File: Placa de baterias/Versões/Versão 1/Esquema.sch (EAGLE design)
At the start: 3 parts

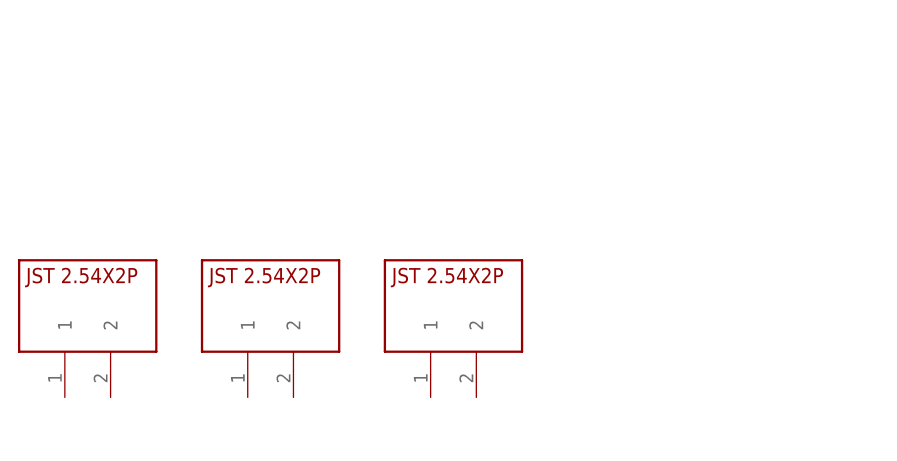
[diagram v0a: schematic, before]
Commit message: mudanças na placa de processamento
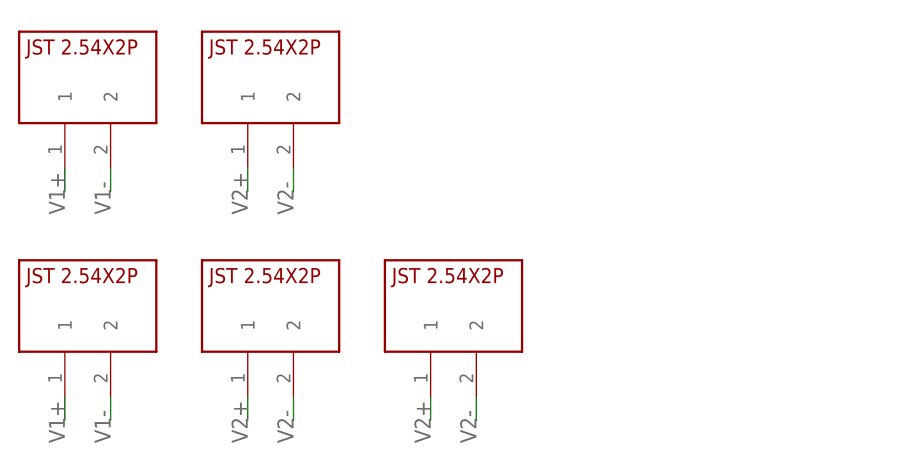
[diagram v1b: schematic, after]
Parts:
- added U$4, U$5: JST2.54X2P, CRD:JST2.54X2P
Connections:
- new net V1+: U$1.1, U$4.1
- new net V1-: U$1.2, U$4.2
- new net V2+: U$2.1, U$3.1, U$5.1
- new net V2-: U$2.2, U$3.2, U$5.2
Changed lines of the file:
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@@
 <part name="U$2" library="CRD" library_urn="urn:adsk.eagle:library:39051337" deviceset="JST2.54X2P" device="" package3d_urn="urn:adsk.eagle:package:39191967/2"/>
 <part name="U$3" library="CRD" library_urn="urn:adsk.eagle:library:39051337" deviceset="JST2.54X2P" device="" package3d_urn="urn:adsk.eagle:package:39191967/2"/>
+<part name="U$4" library="CRD" library_urn="urn:adsk.eagle:library:39051337" deviceset="JST2.54X2P" device="" package3d_urn="urn:adsk.eagle:package:39191967/2"/>
+<part name="U$5" library="CRD" library_urn="urn:adsk.eagle:library:39051337" deviceset="JST2.54X2P" device="" package3d_urn="urn:adsk.eagle:package:39191967/2"/>
 </parts>
 <sheets>
@@
 <instance part="U$2" gate="G$1" x="0" y="0" smashed="yes"/>
 <instance part="U$3" gate="G$1" x="20.32" y="0" smashed="yes"/>
+<instance part="U$4" gate="G$1" x="-20.32" y="25.4" smashed="yes"/>
+<instance part="U$5" gate="G$1" x="0" y="25.4" smashed="yes"/>
 </instances>
 <busses>
 </busses>
 <nets>
+<net name="V1+" class="0">
+<segment>
+<pinref part="U$4" gate="G$1" pin="1"/>
+<wire x1="-22.86" y1="15.24" x2="-22.86" y2="12.7" width="0.1524" layer="91"/>
+<label x="-22.86" y="10.16" size="1.778" layer="95" rot="R90"/>
+</segment>
+<segment>
+<pinref part="U$1" gate="G$1" pin="1"/>
+<wire x1="-22.86" y1="-10.16" x2="-22.86" y2="-12.7" width="0.1524" layer="91"/>
+<label x="-22.86" y="-15.24" size="1.778" layer="95" rot="R90"/>
+</segment>
+</net>
+<net name="V1-" class="0">
+<segment>
+<pinref part="U$4" gate="G$1" pin="2"/>
+<wire x1="-17.78" y1="15.24" x2="-17.78" y2="12.7" width="0.1524" layer="91"/>
+<label x="-17.78" y="10.16" size="1.778" layer="95" rot="R90"/>
+</segment>
+<segment>
+<pinref part="U$1" gate="G$1" pin="2"/>
+<wire x1="-17.78" y1="-10.16" x2="-17.78" y2="-12.7" width="0.1524" layer="91"/>
+<label x="-17.78" y="-15.24" size="1.778" layer="95" rot="R90"/>
+</segment>
+</net>
+<net name="V2+" class="0">
+<segment>
+<pinref part="U$5" gate="G$1" pin="1"/>
+<wire x1="-2.54" y1="15.24" x2="-2.54" y2="12.7" width="0.1524" layer="91"/>
+<label x="-2.54" y="10.16" size="1.778" layer="95" rot="R90"/>
+</segment>
+<segment>
+<pinref part="U$2" gate="G$1" pin="1"/>
+<wire x1="-2.54" y1="-10.16" x2="-2.54" y2="-12.7" width="0.1524" layer="91"/>
+<label x="-2.54" y="-15.24" size="1.778" layer="95" rot="R90"/>
+</segment>
+<segment>
+<pinref part="U$3" gate="G$1" pin="1"/>
+<wire x1="17.78" y1="-10.16" x2="17.78" y2="-12.7" width="0.1524" layer="91"/>
+<label x="17.78" y="-15.24" size="1.778" layer="95" rot="R90"/>
+</segment>
+</net>
+<net name="V2-" class="0">
+<segment>
+<pinref part="U$5" gate="G$1" pin="2"/>
+<wire x1="2.54" y1="15.24" x2="2.54" y2="12.7" width="0.1524" layer="91"/>
+<label x="2.54" y="10.16" size="1.778" layer="95" rot="R90"/>
+</segment>
+<segment>
+<pinref part="U$2" gate="G$1" pin="2"/>
+<wire x1="2.54" y1="-10.16" x2="2.54" y2="-12.7" width="0.1524" layer="91"/>
+<label x="2.54" y="-15.24" size="1.778" layer="95" rot="R90"/>
+</segment>
+<segment>
+<pinref part="U$3" gate="G$1" pin="2"/>
+<wire x1="22.86" y1="-10.16" x2="22.86" y2="-12.7" width="0.1524" layer="91"/>
+<label x="22.86" y="-15.24" size="1.778" layer="95" rot="R90"/>
+</segment>
+</net>
 </nets>
 </sheet>

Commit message: atualização placa de baterias
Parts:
- added V: 22-23-2041, con-molex:22-23-2041
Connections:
- net V1+: now also V-3.S
- net V1-: now also V-4.S
- net V2+: now also V-2.S
- net V2-: now also V-1.S
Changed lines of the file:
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@@
 <drawing>
 <settings>
-<setting alwaysvectorfont="yes"/>
+<setting alwaysvectorfont="no"/>
 <setting verticaltext="up"/>
 </settings>
@@
 <part name="U$4" library="CRD" library_urn="urn:adsk.eagle:library:39051337" deviceset="JST2.54X2P" device="" package3d_urn="urn:adsk.eagle:package:39191967/2"/>
 <part name="U$5" library="CRD" library_urn="urn:adsk.eagle:library:39051337" deviceset="JST2.54X2P" device="" package3d_urn="urn:adsk.eagle:package:39191967/2"/>
+<part name="V" library="con-molex" library_urn="urn:adsk.eagle:library:165" deviceset="22-23-2041" device="" package3d_urn="urn:adsk.eagle:package:8078635/1"/>
 </parts>
 <sheets>
@@
 <instance part="U$4" gate="G$1" x="-20.32" y="25.4" smashed="yes"/>
 <instance part="U$5" gate="G$1" x="0" y="25.4" smashed="yes"/>
+<instance part="V" gate="-1" x="50.8" y="27.94" smashed="yes">
+<attribute name="NAME" x="53.34" y="27.178" size="1.524" layer="95"/>
+<attribute name="VALUE" x="50.038" y="29.337" size="1.778" layer="96"/>
+</instance>
+<instance part="V" gate="-2" x="50.8" y="25.4" smashed="yes">
+<attribute name="NAME" x="53.34" y="24.638" size="1.524" layer="95"/>
+</instance>
+<instance part="V" gate="-3" x="50.8" y="22.86" smashed="yes">
+<attribute name="NAME" x="53.34" y="22.098" size="1.524" layer="95"/>
+</instance>
+<instance part="V" gate="-4" x="50.8" y="20.32" smashed="yes">
+<attribute name="NAME" x="53.34" y="19.558" size="1.524" layer="95"/>
+</instance>
 </instances>
 <busses>
@@
 <label x="-22.86" y="-15.24" size="1.778" layer="95" rot="R90"/>
 </segment>
+<segment>
+<pinref part="V" gate="-3" pin="S"/>
+<wire x1="48.26" y1="22.86" x2="43.18" y2="22.86" width="0.1524" layer="91"/>
+<label x="40.64" y="22.86" size="1.778" layer="95"/>
+</segment>
 </net>
 <net name="V1-" class="0">
@@
 <wire x1="-17.78" y1="-10.16" x2="-17.78" y2="-12.7" width="0.1524" layer="91"/>
 <label x="-17.78" y="-15.24" size="1.778" layer="95" rot="R90"/>
+</segment>
+<segment>
+<pinref part="V" gate="-4" pin="S"/>
+<wire x1="48.26" y1="20.32" x2="43.18" y2="20.32" width="0.1524" layer="91"/>
+<label x="40.64" y="20.32" size="1.778" layer="95"/>
 </segment>
 </net>
@@
 <label x="17.78" y="-15.24" size="1.778" layer="95" rot="R90"/>
 </segment>
+<segment>
+<pinref part="V" gate="-2" pin="S"/>
+<wire x1="48.26" y1="25.4" x2="43.18" y2="25.4" width="0.1524" layer="91"/>
+<label x="40.64" y="25.4" size="1.778" layer="95"/>
+</segment>
 </net>
 <net name="V2-" class="0">
@@
 <label x="22.86" y="-15.24" size="1.778" layer="95" rot="R90"/>
 </segment>
+<segment>
+<pinref part="V" gate="-1" pin="S"/>
+<wire x1="48.26" y1="27.94" x2="43.18" y2="27.94" width="0.1524" layer="91"/>
+<label x="40.64" y="27.94" size="1.778" layer="95"/>
+</segment>
 </net>
